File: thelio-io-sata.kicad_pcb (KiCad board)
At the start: 4 copper layers, 74 x 50 mm, 12 parts

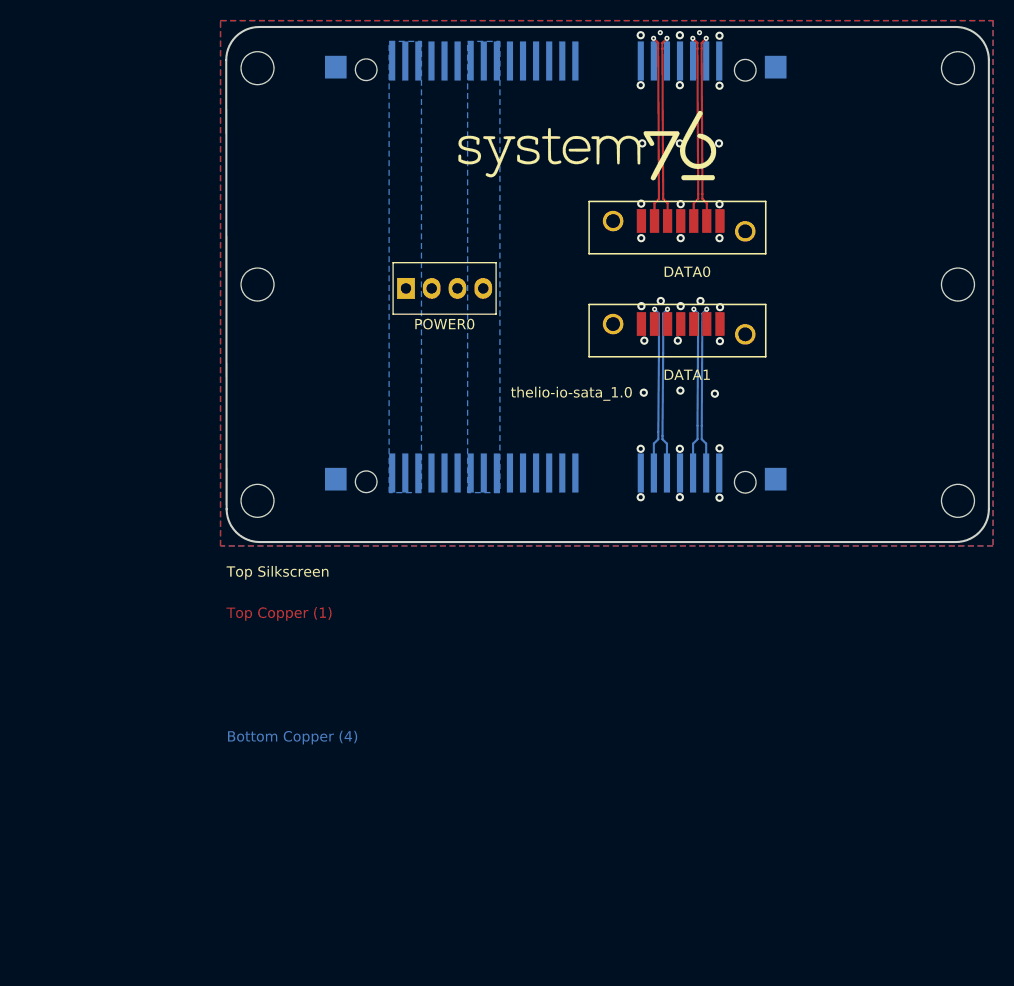
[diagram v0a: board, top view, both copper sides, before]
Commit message: thelio-io-sata 2.0 add SMT standoffs, move connector locations
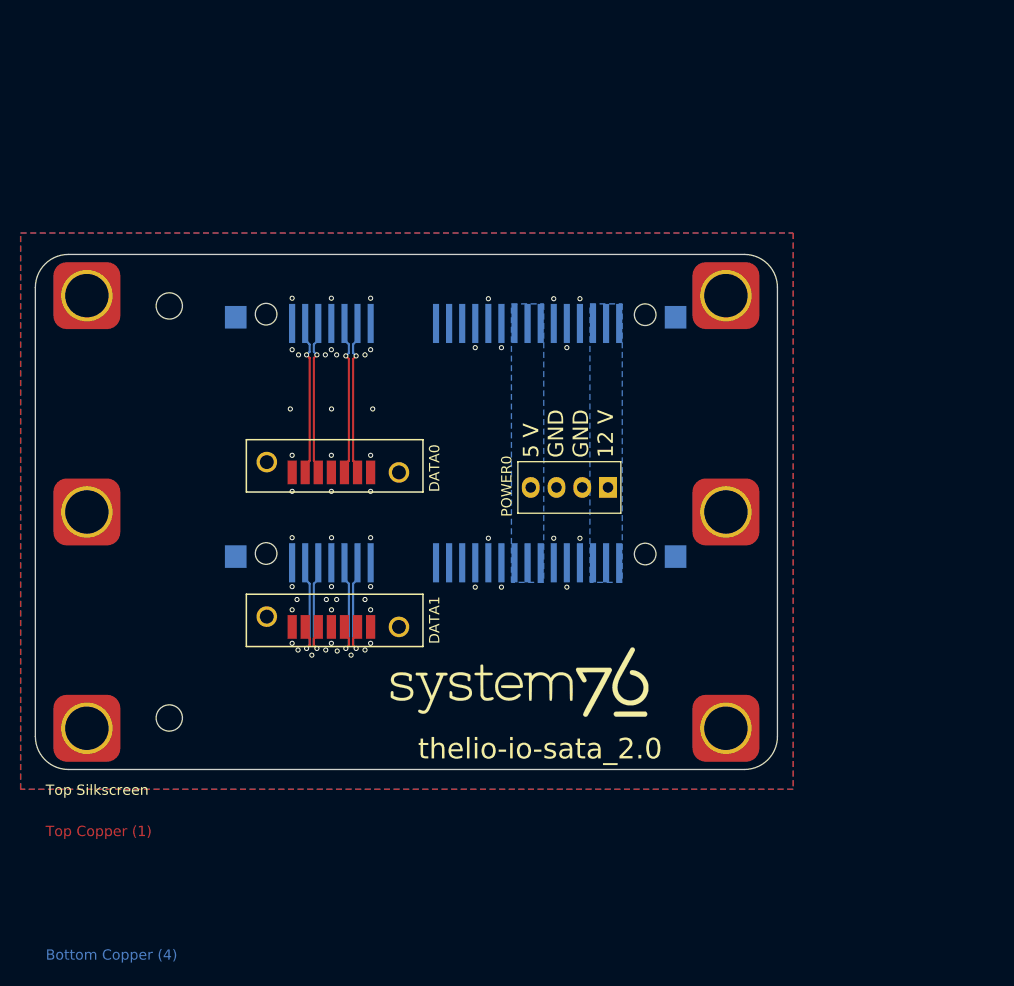
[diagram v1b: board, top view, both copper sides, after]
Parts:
- removed REF** (x6): MountingHole_3.2mm_M3, MountingHole:MountingHole_3.2mm_M3
- added H1: SMTSOM330STR, SMTSO:SMTSO-M3-3, F.Cu at (32.0, 54.0)
- added H2: SMTSOM330STR, SMTSO:SMTSO-M3-3, F.Cu at (94.0, 54.0)
- added H3: SMTSOM330STR, SMTSO:SMTSO-M3-3, F.Cu at (32.0, 75.0)
- added H4: SMTSOM330STR, SMTSO:SMTSO-M3-3, F.Cu at (94.0, 75.0)
- added H5: SMTSOM330STR, SMTSO:SMTSO-M3-3, F.Cu at (32.0, 96.0)
- added H6: SMTSOM330STR, SMTSO:SMTSO-M3-3, F.Cu at (94.0, 96.0)
- added TH?: th, kicad_pcb:tooling_hole_2.55, F.Cu at (40.0, 55.0)
- added TH?: th, kicad_pcb:tooling_hole_2.55, F.Cu at (40.0, 95.0)
- moved G*** 52.5 mm to (74.0, 91.5)
- moved DATA1 49.3 mm to (55.1, 88.7), turned to 180 degrees
- moved DATA0 45.9 mm to (55.1, 73.7), turned to 180 degrees
- moved SATA0 27.3 mm to (67.8, 56.7), turned to 0 degrees
- moved POWER0 22.8 mm to (78.8, 72.6), turned to 180 degrees
- moved SATA1 13.1 mm to (67.8, 79.9), turned to 0 degrees
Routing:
- net /SATA1_B+: track 17.7 -> 11.0 mm
- net /SATA1_B-: track 17.7 -> 11.0 mm
- net /SATA1_A+: track 17.7 -> 11.0 mm
- net /SATA1_A-: track 17.7 -> 11.0 mm
- net /SATA0_B+: track 20.3 -> 15.1 mm
- net /SATA0_A+: track 20.3 -> 15.1 mm
- net /SATA0_A-: track 20.3 -> 15.1 mm
- net /SATA0_B-: track 20.3 -> 15.1 mm
- net GND: track 2.55 -> 0.00 mm, vias 34 -> 53
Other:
- board size 74 x 50 mm -> 72 x 50 mm
- board text added: "5 V GND GND 12 V"
- board text added: "thelio-io-sata_2.0"
- board text added: "thelio-io-sata_2.0 Board must be RoHS compliant Fabricate to IPC-A-600 Class II Material: Shengyi S1000-2 or equivalent Inner copper 1 or 1/2 oz Outer copper, min 33.4 um finished Black LPI solder mask over bare copper Vendor may remove solder mask from via holes, maximum of drill size + 3 mil Finish: OSP Silkscreen: white non conductive 100% electrical test required Remove all unused pads from i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"
- board text removed: "thelio-io-sata_1.0"
- board text removed: "thelio-io-sata_1.0 Board must be RoHS compliant Fabricate to IPC-A-600 Class II Material: Shengyi S1000-2 or equivalent Inner copper 1 or 1/2 oz Outer copper, min 33.4 um finished Black LPI solder mask over bare copper Vendor may remove solder mask from via holes, maximum of drill size + 3 mil Finish: OSP Silkscreen: white non conductive 100% electrical test required Remove all unused pads from i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"
